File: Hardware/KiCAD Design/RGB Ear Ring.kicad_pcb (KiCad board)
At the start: 2 copper layers, 24 x 38 mm, 13 parts, among them J1 AVR-ISP-6, U1 ATtiny85V-10MU

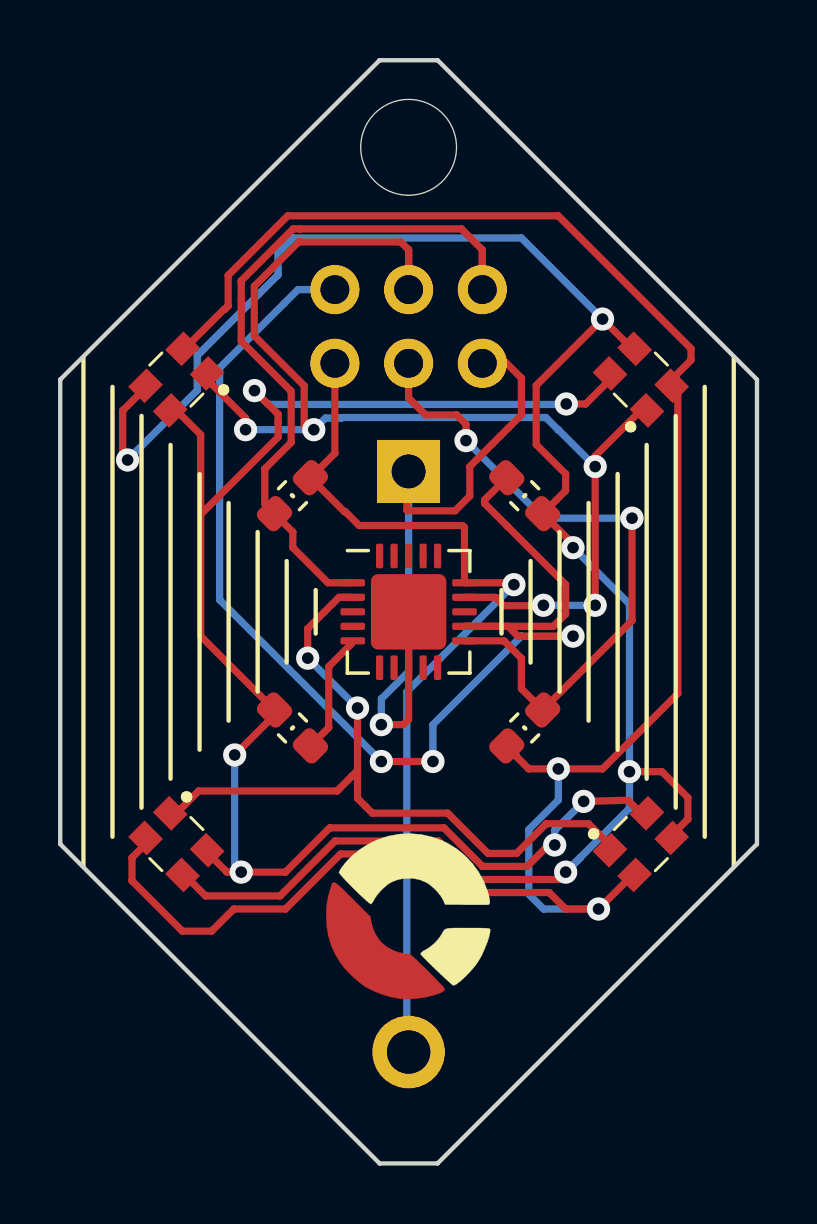
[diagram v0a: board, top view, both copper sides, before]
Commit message: Posted 1051 - (V2.1)
Hardware Update for newer version.  Allows for PWM function on Blue pins.
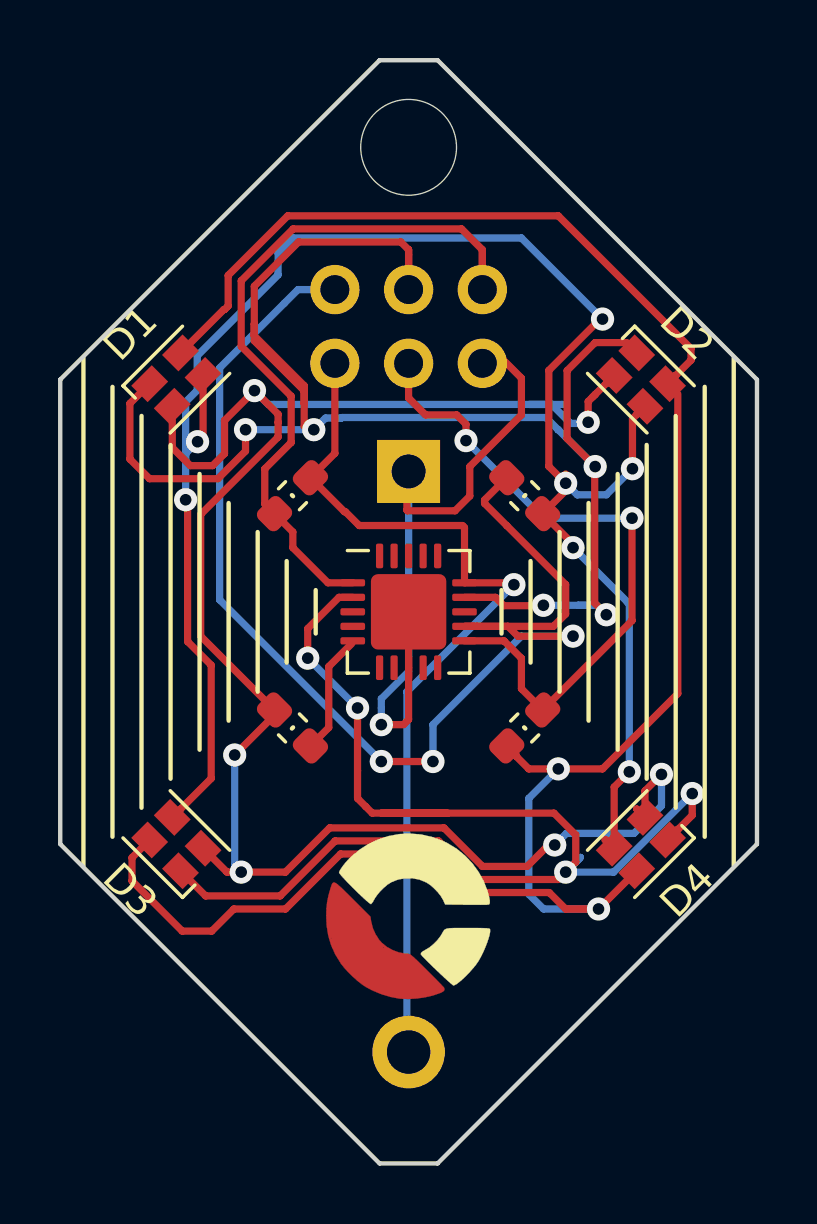
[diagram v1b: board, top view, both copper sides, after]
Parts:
- D1, D2, D3, D4: footprint CCC-Parts-Library:ASMBKTF00A306 -> LED_SMD:LED_Cree-PLCC4_2x2mm_CW
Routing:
- net A1: track 26.0 -> 44.5 mm, vias 2 -> 4
- net A0: track 42.3 -> 57.1 mm
- net R: track 55.1 -> 63.3 mm
- net G: track 70.5 -> 65.5 mm, vias 5 -> 7
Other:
- board text added: "1051"
- board text removed: "1047"
